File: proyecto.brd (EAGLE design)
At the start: 95.8 x 48.2 mm, 42 parts, among them IC1 ADE9153AACPZ, J1 796638-3, K1 PR28-3V-360-1A-E, Q1 12.288M, Q2 BSS123, U1 ESP32-PICO-MINI-02-N8R2ESP32-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

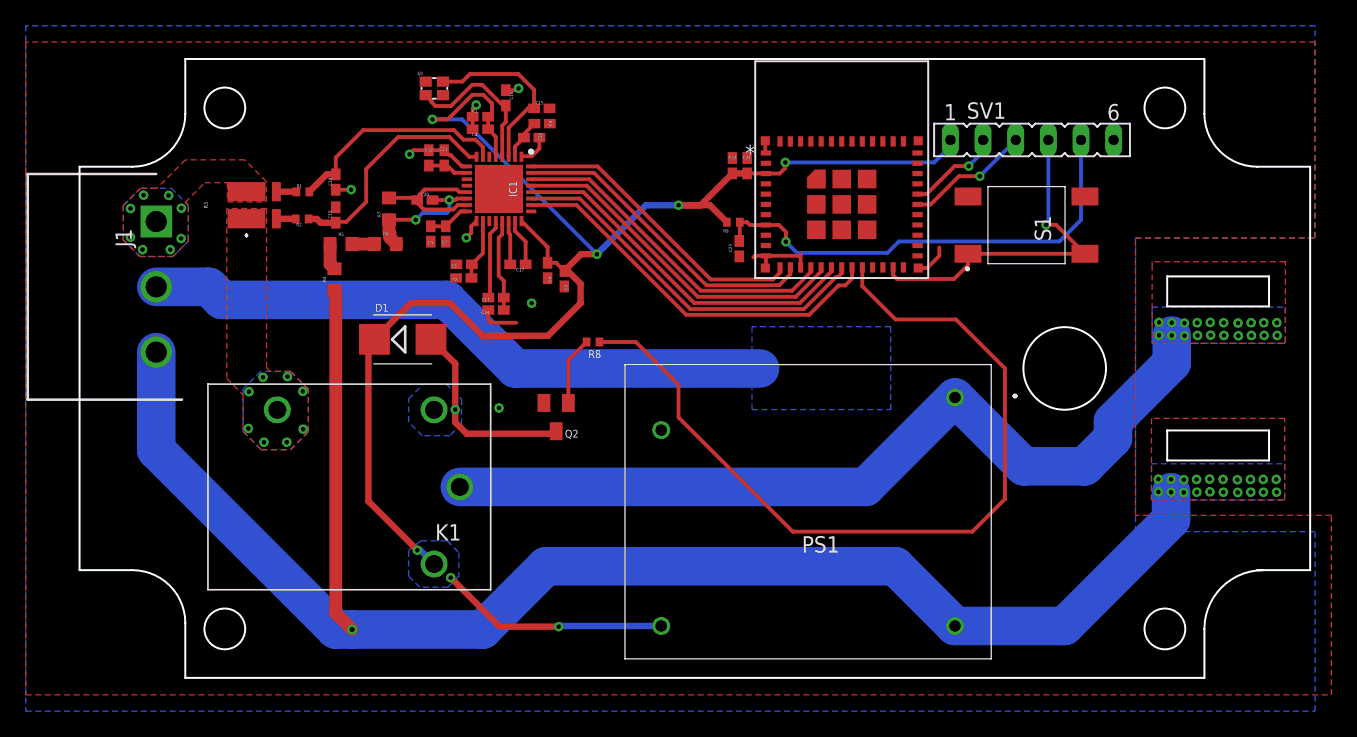
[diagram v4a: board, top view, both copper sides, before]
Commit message: Diseño terminado
Se termino el diseño del esquematico y de la PCB
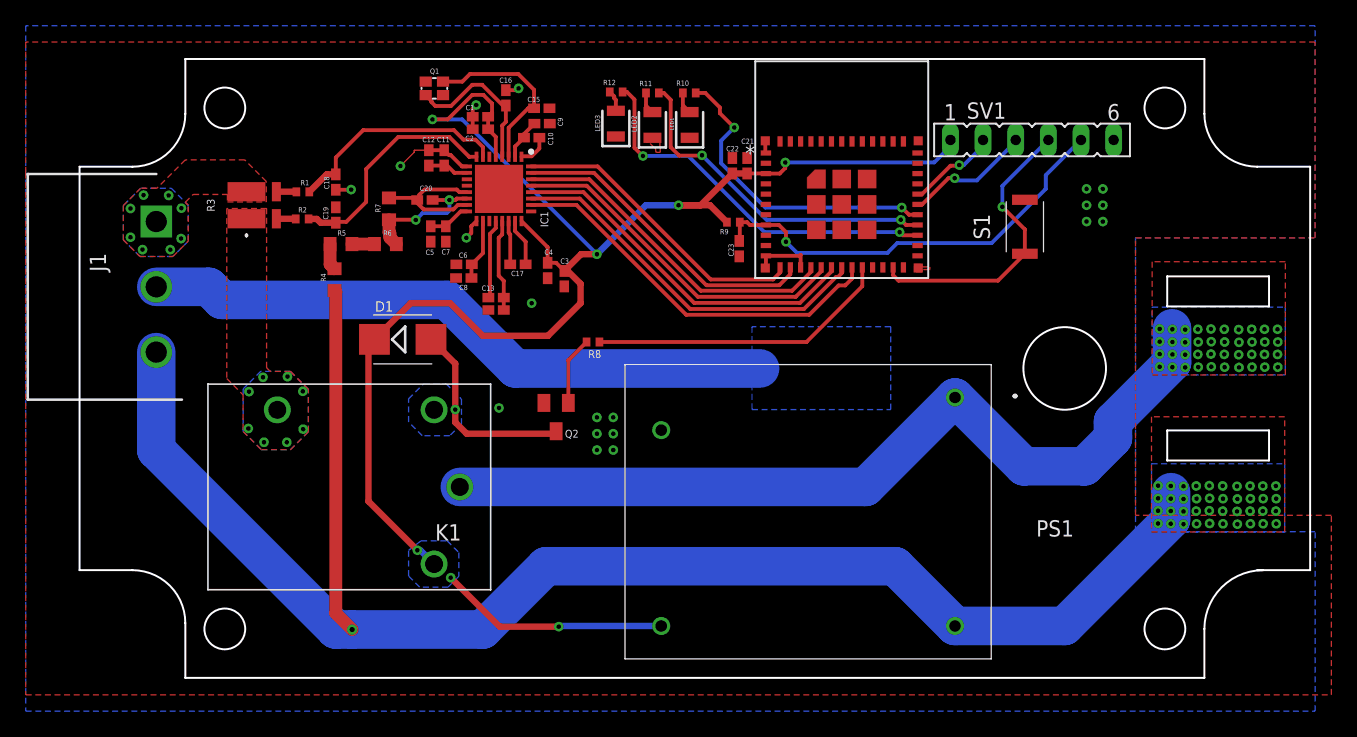
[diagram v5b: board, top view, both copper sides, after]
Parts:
- added LED1: NCD0805R1, SamacSys_Parts:LEDC2012X120N
- added LED2: NCD0805B2, libreria_propia:LEDC2012X120N
- added LED3: NCD0805G1, libreria_propia:LEDC2012X120N
- added R10, R11, R12: 1k, rcl:R0402
- S1: value 3-1437565-0 -> SKRKAEE020; device SamacSys_Parts:314375650 -> SamacSys_Parts:SKRKAEE020
- moved S1 0.18 mm to (25.7, 11.0)
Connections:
- new net LED_B: R11.1, U1.28
- new net LED_G: R12.1, U1.27
- new net LED_R: R10.1, U1.29
- new net N$11: LED1.2, R10.2
- new net N$12: LED2.2, R11.2
- new net N$14: LED3.2, R12.2
- net BOOT: no longer S1.2
- net GND: now also LED1.1, LED2.1, LED3.1, S1.2; no longer S1.3, S1.4
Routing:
- net RELAY_CONTROL: track 65.6 -> 23.7 mm
- net LED_G: track 0.00 -> 29.8 mm, vias 0 -> 2
- net LED_B: track 0.00 -> 26.6 mm, vias 0 -> 2
- net LED_R: track 0.00 -> 24.5 mm, vias 0 -> 2
- net GND: track 32.1 -> 26.5 mm, vias 7 -> 19
- net BOOT: track 27.6 -> 23.0 mm
- net EN: track 36.7 -> 33.7 mm
- net N$11: track 0.00 -> 1.71 mm
- net N$12: track 0.00 -> 1.70 mm
- net N$14: track 0.00 -> 1.66 mm
- net LINEA: track 66.7 -> 67.3 mm, vias 20 -> 40
- net NEUTRO: vias 21 -> 41

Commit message: Se añadieron test pads
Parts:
- added TP1, TP3, TP4: PTR1TP10R, testpad:TP10R
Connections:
- net +3V3: now also TP3.TP
- net GND: now also TP4.TP
- net RELAY_CONTROL: now also TP1.TP
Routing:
- net N$13: track 5.33 -> 0.00 mm
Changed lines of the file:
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@@
 <drawing>
 <settings>
-<setting alwaysvectorfont="no"/>
+<setting alwaysvectorfont="yes"/>
 <setting verticaltext="up"/>
 </settings>
@@
 <attribute name="VALUE" x="-5.2324" y="22.3774" size="0.3048" layer="27" rot="R180"/>
 </element>
+<element name="TP3" library="testpad" library_urn="urn:adsk.eagle:library:385" package="TP10R" package3d_urn="urn:adsk.eagle:package:27959/1" value="PTR1TP10R" x="-25.4" y="-6.35" smashed="yes">
+<attribute name="NAME" x="-26.67" y="-4.699" size="1.27" layer="25" ratio="10"/>
+<attribute name="POPULARITY" value="0" x="-25.4" y="-6.35" size="1.778" layer="27" display="off"/>
+<attribute name="TP_SIGNAL_NAME" value="" x="-25.4" y="-6.35" size="1.778" layer="27" display="off"/>
+<attribute name="VALUE" x="-26.67" y="-7.747" size="0.0254" layer="27"/>
+</element>
+<element name="TP4" library="testpad" library_urn="urn:adsk.eagle:library:385" package="TP10R" package3d_urn="urn:adsk.eagle:package:27959/1" value="PTR1TP10R" x="28.2448" y="-13.0048" smashed="yes">
+<attribute name="NAME" x="26.9748" y="-11.3538" size="1.27" layer="25" ratio="10"/>
+<attribute name="POPULARITY" value="0" x="28.2448" y="-13.0048" size="1.778" layer="27" display="off"/>
+<attribute name="TP_SIGNAL_NAME" value="" x="28.2448" y="-13.0048" size="1.778" layer="27" display="off"/>
+<attribute name="VALUE" x="26.9748" y="-14.4018" size="0.0254" layer="27"/>
+</element>
+<element name="TP1" library="testpad" library_urn="urn:adsk.eagle:library:385" package="TP10R" package3d_urn="urn:adsk.eagle:package:27959/1" value="PTR1TP10R" x="10.2362" y="3.5814" smashed="yes">
+<attribute name="NAME" x="9.7361" y="4.1313" size="1.27" layer="25"/>
+<attribute name="POPULARITY" value="0" x="10.2362" y="3.5814" size="1.778" layer="27" display="off"/>
+<attribute name="TP_SIGNAL_NAME" value="" x="10.2362" y="3.5814" size="1.778" layer="27" display="off"/>
+<attribute name="VALUE" x="9.8552" y="3.0734" size="0.0254" layer="27"/>
+</element>
 </elements>
 <signals>
@@
 <wire x1="-21.8028" y1="16.983" x2="-20.701" y2="16.983" width="0.1016" layer="1"/>
 <contactref element="PS1" pad="2"/>
+<contactref element="TP4" pad="TP"/>
 </signal>
 <signal name="AVDDOUT">
@@
 <wire x1="-25.4" y1="1.27" x2="-25.4" y2="1.7936" width="0.3" layer="1"/>
 <wire x1="-25.4" y1="1.7936" x2="-24.933" y2="2.2606" width="0.3" layer="1"/>
+<contactref element="TP3" pad="TP"/>
+<wire x1="-24.933" y1="2.2606" x2="-25.4" y2="-6.35" width="0" layer="19" extent="1-1"/>
 </signal>
 <signal name="N$1">
@@
 <wire x1="-10.9904" y1="-5.08" x2="-10.795" y2="-4.8846" width="0.5" layer="1"/>
 </signal>
-<signal name="N$13">
-<contactref element="R8" pad="2"/>
-<contactref element="Q2" pad="1"/>
-<wire x1="-9.845" y1="-2.6846" x2="-9.845" y2="0.6372" width="0.3" layer="1"/>
-<wire x1="-9.845" y1="0.6372" x2="-8.4248" y2="2.0574" width="0.3" layer="1"/>
-</signal>
 <signal name="RELAY_CONTROL">
 <contactref element="R8" pad="1"/>
@@
 <wire x1="13.03" y1="6.401" x2="13.03" y2="7.8635" width="0.3" layer="1"/>
 <wire x1="-7.4248" y1="2.0574" x2="8.6864" y2="2.0574" width="0.3" layer="1"/>
-<wire x1="8.6864" y1="2.0574" x2="13.03" y2="6.401" width="0.3" layer="1"/>
+<wire x1="8.6864" y1="2.0574" x2="10.2362" y2="3.6072" width="0.3" layer="1"/>
+<contactref element="TP1" pad="TP"/>
+<wire x1="10.2362" y1="3.5814" x2="10.2362" y2="3.6072" width="0.3" layer="1"/>
+<wire x1="10.2362" y1="3.6072" x2="13.03" y2="6.401" width="0.3" layer="1"/>
 </signal>
 <signal name="EN">
@@
 <wire x1="-4.064" y1="16.5354" x2="-4.699" y2="17.1704" width="0.3" layer="1"/>
 </signal>
+<signal name="N$13">
+<contactref element="R8" pad="2"/>
+<contactref element="Q2" pad="1"/>
+<wire x1="-8.4248" y1="2.0574" x2="-9.845" y2="-2.6846" width="0" layer="19" extent="1-1"/>
+</signal>
 </signals>

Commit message: Finalizado
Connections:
- net MONDA renamed CARGA-M
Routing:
- net +3V3: track 132.6 -> 140.2 mm
- net N$13: track 0.00 -> 5.33 mm

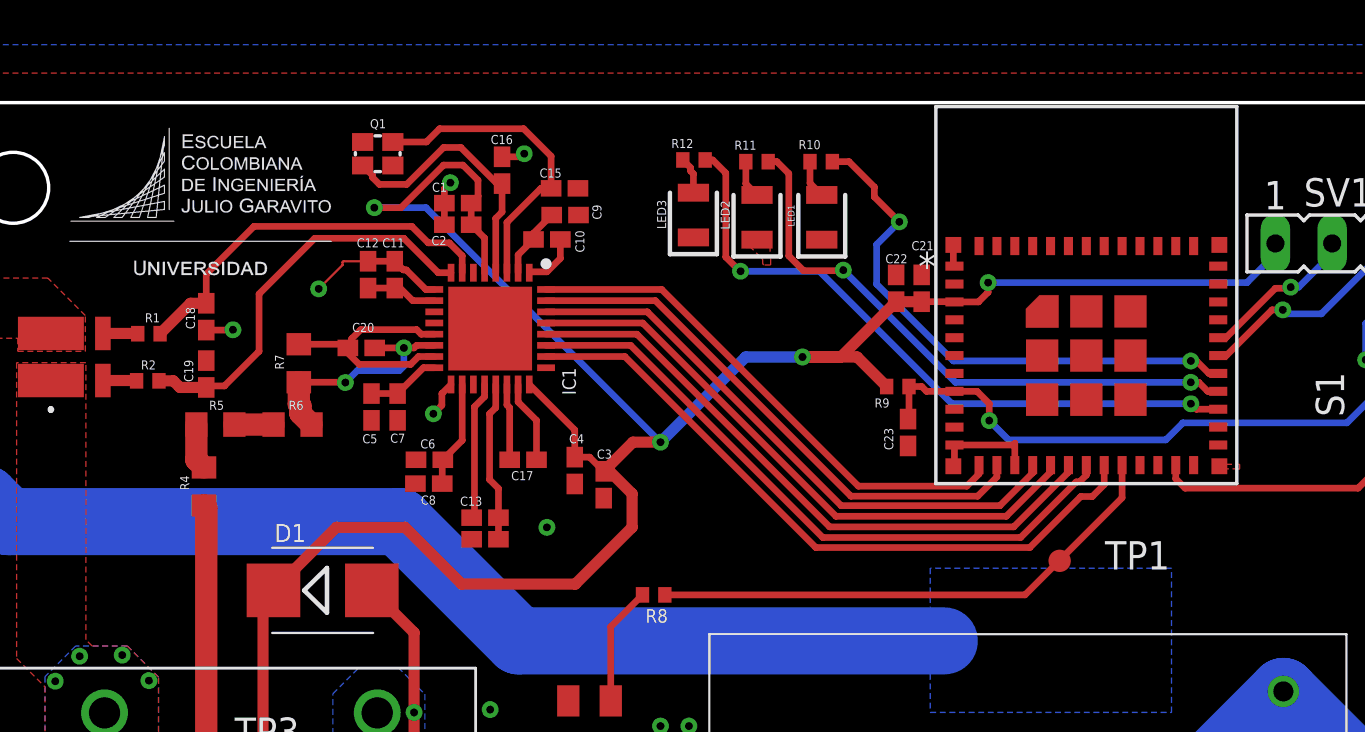
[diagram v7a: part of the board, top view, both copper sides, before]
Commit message: Adicion de pistas faltantes
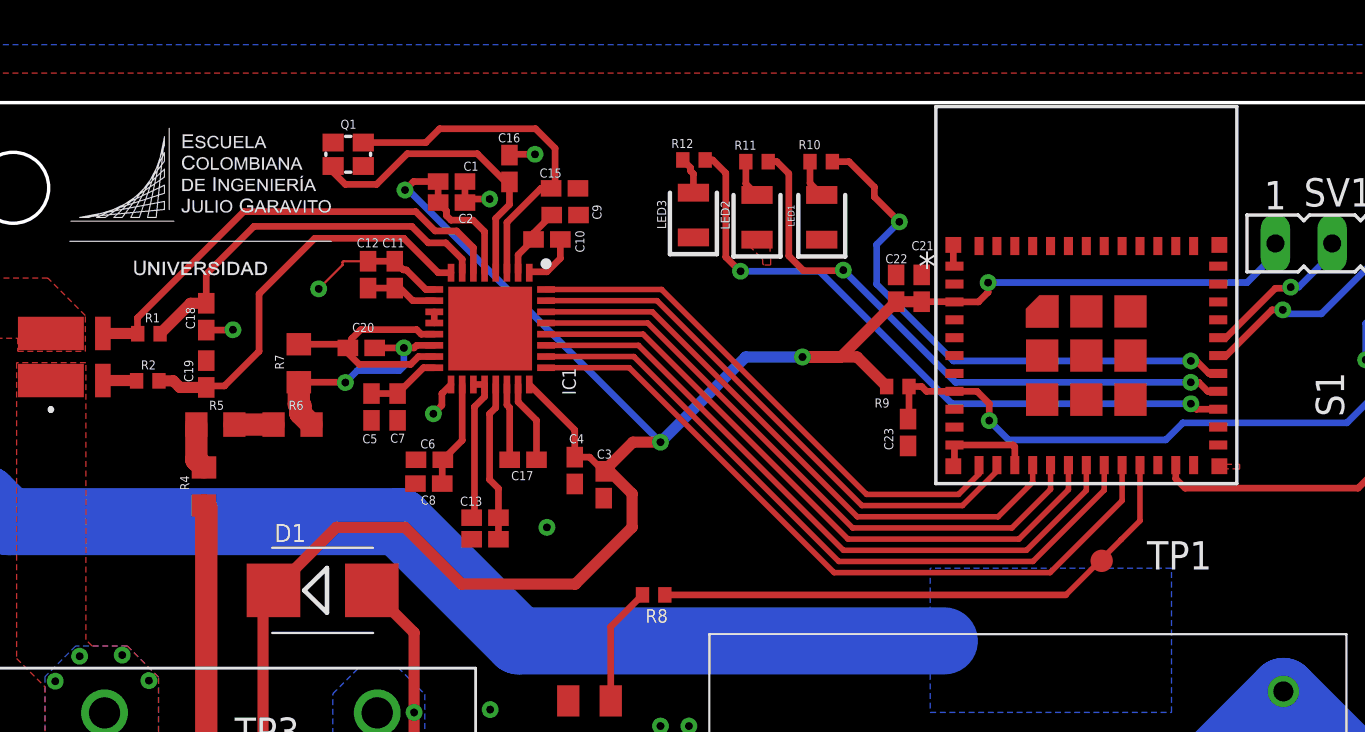
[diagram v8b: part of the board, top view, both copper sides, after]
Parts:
- moved TP1 1.88 mm to (12.1, 3.58)
- moved Q1 1.32 mm to (-21.6, 21.8)
- moved C2 1.03 mm to (-17.0, 19.6), turned to 0 degrees
- moved C1 1.00 mm to (-17.0, 20.5), turned to 0 degrees
- moved C16 0.34 mm to (-14.4, 21.1)
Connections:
- new net CF2: IC1.25, U1.20
- new net N$16: IC1.11, IC1.12
- net GND: now also IC1.19
- net N$2: now also IC1.6
- net RELAY_CONTROL: now also U1.21; no longer U1.20
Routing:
- net CF2: track 0.00 -> 32.5 mm
- net N$2: track 1.56 -> 21.0 mm
- net +3V3: track 140.2 -> 136.1 mm
- net CLKOUT: track 14.1 -> 15.9 mm
- net CLKIN: track 12.1 -> 13.8 mm
- net RELAY_CONTROL: track 23.7 -> 25.2 mm
- net RESET: track 28.3 -> 29.2 mm
- net RX: track 27.3 -> 28.2 mm
- net IRQ: track 29.3 -> 30.2 mm
- net CF1: track 30.5 -> 31.2 mm
- net TX: track 26.3 -> 27.0 mm
- net GND: track 26.5 -> 27.1 mm
- net N$16: track 0.00 -> 0.50 mm
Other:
- board text added: "Tomas Felipe Montañez Piñeros Juan Andrés Rodriguez Ruiz Juan Andrés Abella Ballén"
